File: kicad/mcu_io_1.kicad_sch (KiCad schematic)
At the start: 6 parts, among them SW1 SW_SPST, U7 MCXN947VDFT, Y1 24MHz

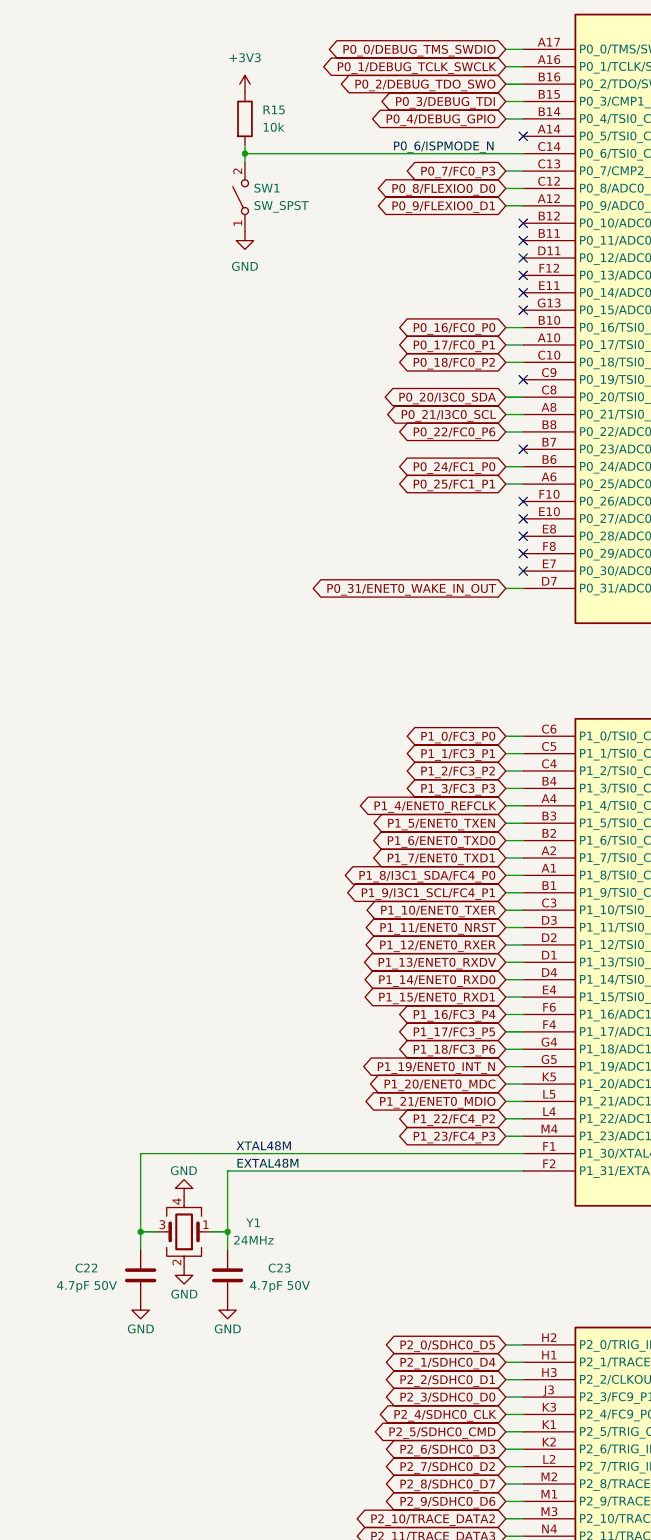
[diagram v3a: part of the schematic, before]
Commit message: Updated schematic after feedback from Jari
- Finished schematic after feedback from Jari. It is at a finished state, can be reviewed by whole team now.
- Layouted MCXN with decoupling caps.
- Layouted Base100-T1 ethernet phy.
- Layouted the power supply a bit.
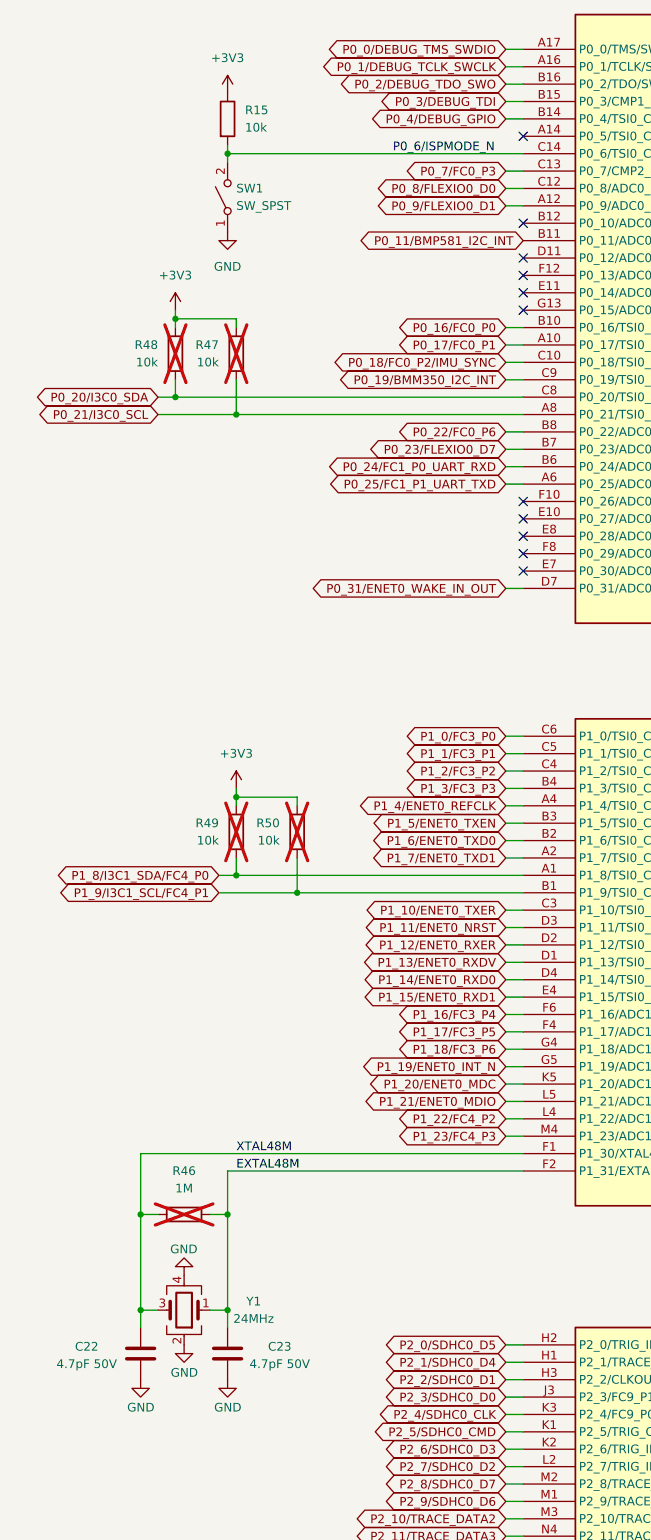
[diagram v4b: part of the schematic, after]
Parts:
- added R46: 1M, symbol Device:R
- added R47, R48, R49, R50: 10k, symbol Device:R
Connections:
- net +3V3: now also R47.1, R48.1, R49.1, R50.1
- net EXTAL48M: now also R46.2
- net P0_20/I3C0_SDA: now also R48.2
- net P0_21/I3C0_SCL: now also R47.2
- net P1_8/I3C1_SDA/FC4_P0: now also R49.2
- net P1_9/I3C1_SCL/FC4_P1: now also R50.2
- net XTAL48M: now also R46.1
- net P0_11/BMP581_I2C_INT: now reaches U7.B11 (P0_11/ADC0_B11/CT0_MAT1/FLEXIO0_D3/HSCMP2_OUT)
- net P0_23/FLEXIO0_D7: now reaches U7.B7 (P0_23/ADC0_A15/CMP2_IN2/EWM0_OUT_b/FC1_P3/CT_INP3/FLEXIO0_D7/WUU0_IN5)
- net P0_19/BMM350_I2C_INT: now reaches U7.C9 (P0_19/TSI0_CH14/ADC0_A11/EWM0_OUT_b/FC0_P3/CT0_MAT3/FLEXIO0_D3/HSCMP1_OUT/WUU0_IN3)
- net P0_18/FC0_P2 renamed P0_18/FC0_P2/IMU_SYNC
- net P0_24/FC1_P0 renamed P0_24/FC1_P0_UART_RXD
- net P0_25/FC1_P1 renamed P0_25/FC1_P1_UART_TXD
- no-connect marks 14 -> 11
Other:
- title: MR-MCXN-T1 Sensor hub -> MR-MCXN-T1 Sensor Node
- moved on the sheet: C22, C23, R15, SW1, Y1

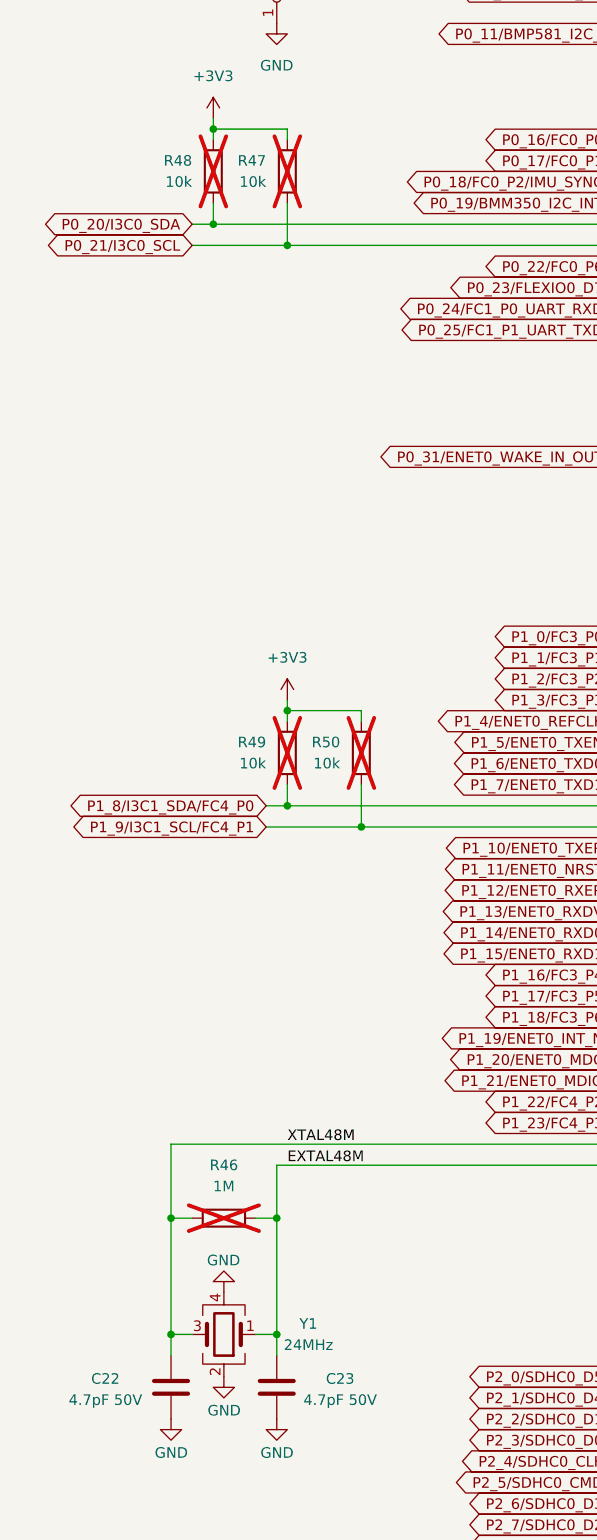
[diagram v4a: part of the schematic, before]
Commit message: Finished schematic. Completed power and ENET phy layout.
Layouted power supply and ethernet phy around input connector.
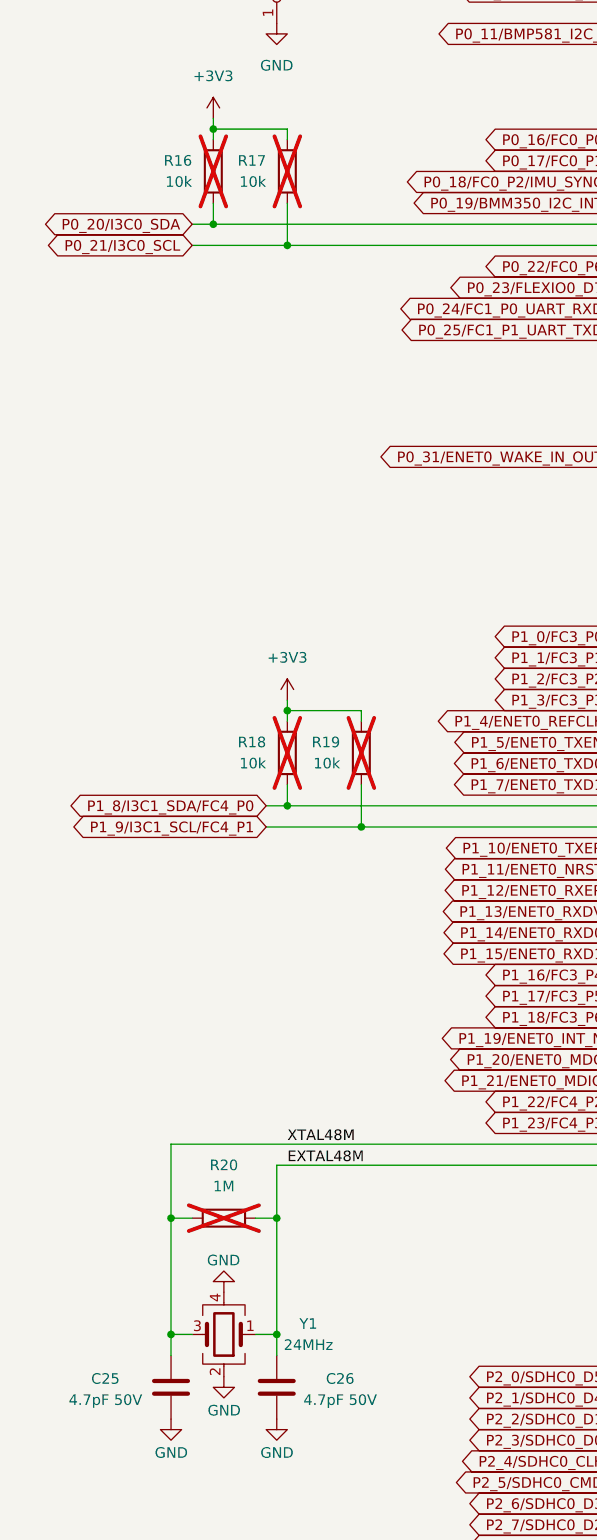
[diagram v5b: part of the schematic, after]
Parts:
- R16: renamed from R48; footprint (none) -> Resistor_SMD:R_0402_1005Metric; MF (none) -> UNI-ROYAL(Uniroyal Elec); MFPN (none) -> 0402WGF1002TCE; Supplier (none) -> JLCPCB; Supplier PN (none) -> C25744
- R17: renamed from R47; footprint (none) -> Resistor_SMD:R_0402_1005Metric; MF (none) -> UNI-ROYAL(Uniroyal Elec); MFPN (none) -> 0402WGF1002TCE; Supplier (none) -> JLCPCB; Supplier PN (none) -> C25744
- R18: renamed from R49; footprint (none) -> Resistor_SMD:R_0402_1005Metric; MF (none) -> UNI-ROYAL(Uniroyal Elec); MFPN (none) -> 0402WGF1002TCE; Supplier (none) -> JLCPCB; Supplier PN (none) -> C25744
- R19: renamed from R50; footprint (none) -> Resistor_SMD:R_0402_1005Metric; MF (none) -> UNI-ROYAL(Uniroyal Elec); MFPN (none) -> 0402WGF1002TCE; Supplier (none) -> JLCPCB; Supplier PN (none) -> C25744
- R20: renamed from R46; footprint (none) -> Resistor_SMD:R_0402_1005Metric; MF (none) -> UNI-ROYAL(Uniroyal Elec); MFPN (none) -> 0402WGF1004TCE; Supplier (none) -> JLCPCB; Supplier PN (none) -> C26083
- renumbered C22 to C25, C23 to C26
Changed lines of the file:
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@@
 		(on_board yes)
 		(dnp no)
-		(property "Reference" "#PWR052"
+		(property "Reference" "#PWR053"
 			(at 49.53 219.71 0)
 			(effects
@@
 			(project "spinali_mcxn_t1_sensor_hub"
 				(path "/8b469ec1-e800-4d46-8a32-95d77ceae6db/2f800241-08a7-49e7-97bc-35e3807b9c21"
-					(reference "#PWR052")
+					(reference "#PWR053")
 					(unit 1)
 				)
@@
 		(dnp no)
 		(fields_autoplaced yes)
-		(property "Reference" "#PWR049"
+		(property "Reference" "#PWR048"
 			(at 55.88 34.29 0)
 			(effects
@@
 			(project "spinali_mcxn_t1_sensor_hub"
 				(path "/8b469ec1-e800-4d46-8a32-95d77ceae6db/2f800241-08a7-49e7-97bc-35e3807b9c21"
-					(reference "#PWR049")
+					(reference "#PWR048")
 					(unit 1)
 				)
@@
 		(on_board yes)
 		(dnp no)
-		(property "Reference" "#PWR051"
+		(property "Reference" "#PWR052"
 			(at 49.53 196.85 0)
 			(effects
@@
 			(project "spinali_mcxn_t1_sensor_hub"
 				(path "/8b469ec1-e800-4d46-8a32-95d77ceae6db/2f800241-08a7-49e7-97bc-35e3807b9c21"
-					(reference "#PWR051")
+					(reference "#PWR052")
 					(unit 1)
 				)
@@
 		(dnp no)
 		(fields_autoplaced yes)
-		(property "Reference" "#PWR0237"
+		(property "Reference" "#PWR051"
 			(at 57.15 135.89 0)
 			(effects
@@
 			(project "spinali_mcxn_t1_sensor_hub"
 				(path "/8b469ec1-e800-4d46-8a32-95d77ceae6db/2f800241-08a7-49e7-97bc-35e3807b9c21"
-					(reference "#PWR0237")
+					(reference "#PWR051")
 					(unit 1)
 				)
@@
 		(on_board yes)
 		(dnp no)
-		(property "Reference" "#PWR053"
+		(property "Reference" "#PWR054"
 			(at 43.18 224.79 0)
 			(effects
@@
 			(project "spinali_mcxn_t1_sensor_hub"
 				(path "/8b469ec1-e800-4d46-8a32-95d77ceae6db/2f800241-08a7-49e7-97bc-35e3807b9c21"
-					(reference "#PWR053")
+					(reference "#PWR054")
 					(unit 1)
 				)
@@
 		(dnp no)
 		(fields_autoplaced yes)
-		(property "Reference" "#PWR050"
+		(property "Reference" "#PWR049"
 			(at 55.88 57.15 0)
 			(effects
@@
 			(project ""
 				(path "/8b469ec1-e800-4d46-8a32-95d77ceae6db/2f800241-08a7-49e7-97bc-35e3807b9c21"
-					(reference "#PWR050")
+					(reference "#PWR049")
 					(unit 1)
 				)
@@
 		(dnp no)
 		(fields_autoplaced yes)
-		(property "Reference" "#PWR0236"
+		(property "Reference" "#PWR050"
 			(at 48.26 66.04 0)
 			(effects
@@
 			(project "spinali_mcxn_t1_sensor_hub"
 				(path "/8b469ec1-e800-4d46-8a32-95d77ceae6db/2f800241-08a7-49e7-97bc-35e3807b9c21"
-					(reference "#PWR0236")
+					(reference "#PWR050")
 					(unit 1)
 				)
@@
 		(on_board yes)
 		(dnp yes)
-		(property "Reference" "R49"
+		(property "Reference" "R18"
 			(at 54.61 137.1599 0)
 			(effects
@@
 			)
 		)
-		(property "Footprint" ""
+		(property "Footprint" "Resistor_SMD:R_0402_1005Metric"
 			(at 58.928 138.43 90)
 			(effects
@@
 			)
 		)
+		(property "MF" "UNI-ROYAL(Uniroyal Elec)"
+			(at 57.15 138.43 0)
+			(effects
+				(font
+					(size 1.27 1.27)
+				)
+				(hide yes)
+			)
+		)
+		(property "MFPN" "0402WGF1002TCE"
+			(at 57.15 138.43 0)
+			(effects
+				(font
+					(size 1.27 1.27)
+				)
+				(hide yes)
+			)
+		)
+		(property "Supplier" "JLCPCB"
+			(at 57.15 138.43 0)
+			(effects
+				(font
+					(size 1.27 1.27)
+				)
+				(hide yes)
+			)
+		)
+		(property "Supplier PN" "C25744"
+			(at 57.15 138.43 0)
+			(effects
+				(font
+					(size 1.27 1.27)
+				)
+				(hide yes)
+			)
+		)
 		(pin "1"
 		)
@@
 			(project "spinali_mcxn_t1_sensor_hub"
 				(path "/8b469ec1-e800-4d46-8a32-95d77ceae6db/2f800241-08a7-49e7-97bc-35e3807b9c21"
-					(reference "R49")
+					(reference "R18")
 					(unit 1)
 				)
@@
 		(on_board yes)
 		(dnp yes)
-		(property "Reference" "R48"
+		(property "Reference" "R16"
 			(at 45.72 67.3099 0)
 			(effects
@@
 			)
 		)
-		(property "Footprint" ""
+		(property "Footprint" "Resistor_SMD:R_0402_1005Metric"
 			(at 50.038 68.58 90)
 			(effects
@@
 			)
 		)
+		(property "MF" "UNI-ROYAL(Uniroyal Elec)"
+			(at 48.26 68.58 0)
+			(effects
+				(font
+					(size 1.27 1.27)
+				)
+				(hide yes)
+			)
+		)
+		(property "MFPN" "0402WGF1002TCE"
+			(at 48.26 68.58 0)
+			(effects
+				(font
+					(size 1.27 1.27)
+				)
+				(hide yes)
+			)
+		)
+		(property "Supplier" "JLCPCB"
+			(at 48.26 68.58 0)
+			(effects
+				(font
+					(size 1.27 1.27)
+				)
+				(hide yes)
+			)
+		)
+		(property "Supplier PN" "C25744"
+			(at 48.26 68.58 0)
+			(effects
+				(font
+					(size 1.27 1.27)
+				)
+				(hide yes)
+			)
+		)
 		(pin "1"
 		)
@@
 			(project ""
 				(path "/8b469ec1-e800-4d46-8a32-95d77ceae6db/2f800241-08a7-49e7-97bc-35e3807b9c21"
-					(reference "R48")
+					(reference "R16")
 					(unit 1)
 				)
@@
 		(on_board yes)
 		(dnp yes)
-		(property "Reference" "R47"
+		(property "Reference" "R17"
 			(at 54.61 67.3099 0)
 			(effects
@@
 			)
 		)
-		(property "Footprint" ""
+		(property "Footprint" "Resistor_SMD:R_0402_1005Metric"
 			(at 55.372 68.58 90)
 			(effects
@@
 			)
 		)
+		(property "MF" "UNI-ROYAL(Uniroyal Elec)"
+			(at 57.15 68.58 0)
+			(effects
+				(font
+					(size 1.27 1.27)
+				)
+				(hide yes)
+			)
+		)
+		(property "MFPN" "0402WGF1002TCE"
+			(at 57.15 68.58 0)
+			(effects
+				(font
+					(size 1.27 1.27)
+				)
+				(hide yes)
+			)
+		)
+		(property "Supplier" "JLCPCB"
+			(at 57.15 68.58 0)
+			(effects
+				(font
+					(size 1.27 1.27)
+				)
+				(hide yes)
+			)
+		)
+		(property "Supplier PN" "C25744"
+			(at 57.15 68.58 0)
+			(effects
+				(font
+					(size 1.27 1.27)
+				)
+				(hide yes)
+			)
+		)
 		(pin "1"
 		)
@@
 			(project ""
 				(path "/8b469ec1-e800-4d46-8a32-95d77ceae6db/2f800241-08a7-49e7-97bc-35e3807b9c21"
-					(reference "R47")
+					(reference "R17")
 					(unit 1)
 				)
@@
 		(on_board yes)
 		(dnp no)
-		(property "Reference" "C22"
+		(property "Reference" "C25"
 			(at 35.306 213.614 0)
 			(effects
@@
 			(project ""
 				(path "/8b469ec1-e800-4d46-8a32-95d77ceae6db/2f800241-08a7-49e7-97bc-35e3807b9c21"
-					(reference "C22")
+					(reference "C25")
 					(unit 1)
 				)
@@
 		(on_board yes)
 		(dnp no)
-		(property "Reference" "C23"
+		(property "Reference" "C26"
 			(at 63.5 213.614 0)
 			(effects
@@
 			(project ""
 				(path "/8b469ec1-e800-4d46-8a32-95d77ceae6db/2f800241-08a7-49e7-97bc-35e3807b9c21"
-					(reference "C23")
+					(reference "C26")
 					(unit 1)
 				)
@@
 		(dnp yes)
 		(fields_autoplaced yes)
-		(property "Reference" "R46"
+		(property "Reference" "R20"
 			(at 49.53 187.96 90)
 			(effects
@@
 			)
 		)
-		(property "Footprint" ""
+		(property "Footprint" "Resistor_SMD:R_0402_1005Metric"
 			(at 49.53 196.088 90)
 			(effects
@@
 			)
 		)
+		(property "MF" "UNI-ROYAL(Uniroyal Elec)"
+			(at 49.53 194.31 0)
+			(effects
+				(font
+					(size 1.27 1.27)
+				)
+				(hide yes)
+			)
+		)
+		(property "MFPN" "0402WGF1004TCE"
+			(at 49.53 194.31 0)
+			(effects
+				(font
+					(size 1.27 1.27)
+				)
+				(hide yes)
+			)
+		)
+		(property "Supplier" "JLCPCB"
+			(at 49.53 194.31 0)
+			(effects
+				(font
+					(size 1.27 1.27)
+				)
+				(hide yes)
+			)
+		)
+		(property "Supplier PN" "C26083"
+			(at 49.53 194.31 0)
+			(effects
+				(font
+					(size 1.27 1.27)
+				)
+				(hide yes)
+			)
+		)
 		(pin "2"
 		)
@@
 			(project ""
 				(path "/8b469ec1-e800-4d46-8a32-95d77ceae6db/2f800241-08a7-49e7-97bc-35e3807b9c21"
-					(reference "R46")
+					(reference "R20")
 					(unit 1)
 				)
@@
 		(on_board yes)
 		(dnp yes)
-		(property "Reference" "R50"
+		(property "Reference" "R19"
 			(at 63.5 137.1599 0)
 			(effects
@@
 			)
 		)
-		(property "Footprint" ""
+		(property "Footprint" "Resistor_SMD:R_0402_1005Metric"
 			(at 64.262 138.43 90)
 			(effects
@@
 			)
 		)
+		(property "MF" "UNI-ROYAL(Uniroyal Elec)"
+			(at 66.04 138.43 0)
+			(effects
+				(font
+					(size 1.27 1.27)
+				)
+				(hide yes)
+			)
+		)
+		(property "MFPN" "0402WGF1002TCE"
+			(at 66.04 138.43 0)
+			(effects
+				(font
+					(size 1.27 1.27)
+				)
+				(hide yes)
+			)
+		)
+		(property "Supplier" "JLCPCB"
+			(at 66.04 138.43 0)
+			(effects
+				(font
+					(size 1.27 1.27)
+				)
+				(hide yes)
+			)
+		)
+		(property "Supplier PN" "C25744"
+			(at 66.04 138.43 0)
+			(effects
+				(font
+					(size 1.27 1.27)
+				)
+				(hide yes)
+			)
+		)
 		(pin "1"
 		)
@@
 			(project "spinali_mcxn_t1_sensor_hub"
 				(path "/8b469ec1-e800-4d46-8a32-95d77ceae6db/2f800241-08a7-49e7-97bc-35e3807b9c21"
-					(reference "R50")
+					(reference "R19")
 					(unit 1)
 				)
@@
 		(on_board yes)
 		(dnp no)
-		(property "Reference" "#PWR054"
+		(property "Reference" "#PWR055"
 			(at 55.88 224.79 0)
 			(effects
@@
 			(project "spinali_mcxn_t1_sensor_hub"
 				(path "/8b469ec1-e800-4d46-8a32-95d77ceae6db/2f800241-08a7-49e7-97bc-35e3807b9c21"
-					(reference "#PWR054")
+					(reference "#PWR055")
 					(unit 1)
 				)

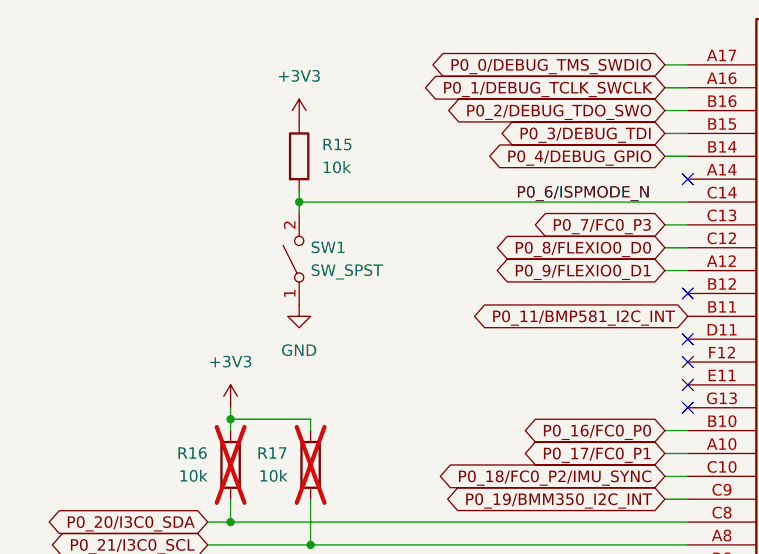
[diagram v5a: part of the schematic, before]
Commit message: Updated layout and BOM
- Flipped Magnetometer so it is aligned with the axis of the IMU.
- Updated BOM so all parts can be sourced from DigiKey. Also added a row for JLCPCB part numbers if applicable.
- Replaced ISP button with the NanoT160AS. Added "ISP" in silkscreen at that button.
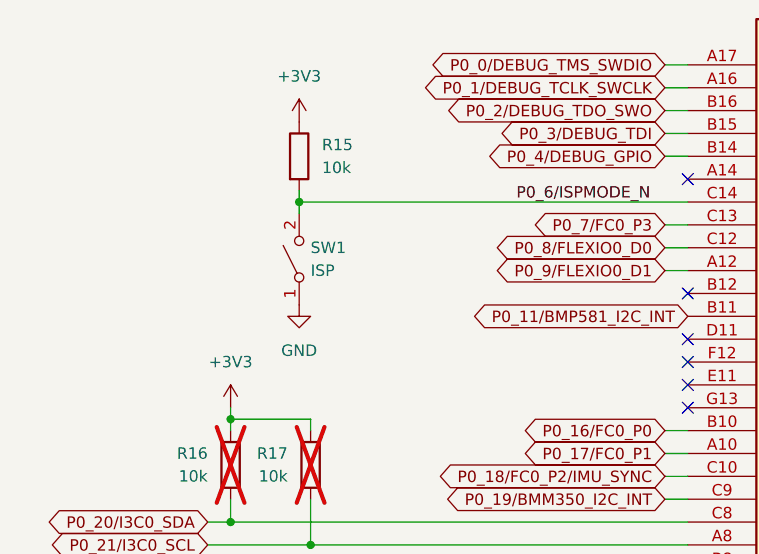
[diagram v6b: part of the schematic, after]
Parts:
- C25, C26: DigiKey (none) -> 490-8102-1-ND; JLCPCB (none) -> C161327; Supplier JLCPCB -> (none); Supplier PN C161327 -> (none)
- R15: DigiKey (none) -> YAG3436CT-ND; JLCPCB (none) -> C144807; MF UNI-ROYAL(Uniroyal Elec) -> YAGEO; MFPN 0402WGF1002TCE -> AC0402FR-0710KL; Supplier JLCPCB -> (none); Supplier PN C25744 -> (none)
- R16, R17, R18, R19: Supplier JLCPCB -> (none); Supplier PN C25744 -> (none)
- R20: Supplier JLCPCB -> (none); Supplier PN C26083 -> (none)
- SW1: value SW_SPST -> ISP; footprint Switches:TS2306A -> Switches:NanoTxxxAS; DigiKey (none) -> 108-NANOT160ASCT-ND; JLCPCB (none) -> C2760981; MF SHOU HAN -> C&K; MFPN TS2306A 200gf 002 -> NANOT160AS; Supplier JLCPCB -> (none); Supplier PN C5363482 -> (none)
- U7: DigiKey (none) -> 568-MCXN947VDFT-ND; JLCPCB (none) -> -; Supplier DigiKey -> (none); Supplier PN 568-MCXN947VDFT-ND -> (none)
- Y1: DigiKey (none) -> 1923-830108212309CT-ND; JLCPCB (none) -> -; Supplier DigiKey -> (none); Supplier PN 1923-830108212309CT-ND -> (none)
